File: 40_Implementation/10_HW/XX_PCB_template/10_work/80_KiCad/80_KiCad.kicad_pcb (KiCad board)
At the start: 4 copper layers, 68.6 x 53.3 mm, 37 parts, among them J1 Power, J2 Digital/PWM, J3 Analog, J4 Digital/PWM, J5 Conn_01x03_Socket, SW1 SW_SPST, U1 OPA340P, U2 OPA340P

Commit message: v1.1
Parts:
- added A2_Out1: TP_Vout2, Connector_PinHeader_2.54mm:PinHeader_1x01_P2.54mm_Vertical, F.Cu at (112.6, 97.1)
- added A_In1_N1: TP_A_in1_N, Connector_PinHeader_2.54mm:PinHeader_1x01_P2.54mm_Vertical, F.Cu at (102.5, 65.8)
- added A_In2_N1: TP_A_in2_N, Connector_PinHeader_2.54mm:PinHeader_1x01_P2.54mm_Vertical, F.Cu at (104.8, 96.9)
- added A_In_P1: TP_A_in_P, Connector_PinHeader_2.54mm:PinHeader_1x01_P2.54mm_Vertical, F.Cu at (102.8, 88.3)
- A1_Out1: value Vout Intermediate -> TP_Vout1
- GND2, GND3: value GND -> TP_GND
- V_In1: value Vin -> TP_Vin
- V_Out1: value Vout -> TP_Vout
- moved V_Out1 19.3 mm to (121.9, 97.5)
- moved GND3 9.60 mm to (102.6, 74.9)
- moved GND1 7.91 mm to (102.9, 59.1)
- moved A1_Out1 6.48 mm to (102.8, 82.5)
- moved VCC1 6.11 mm to (102.8, 52.4)
- moved D1 1.77 mm to (108.0, 54.4), turned to 0 degrees
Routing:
- net Net-(U1--): track 20.3 -> 58.6 mm
- net Net-(A2_Out1-Pad1): track 22.0 -> 52.2 mm
- net Net-(U2--): track 50.9 -> 75.9 mm
- net Vout: track 54.4 -> 36.6 mm
- net Net-(U1-+): track 92.1 -> 105.6 mm
- net Net-(A1_Out1-Pad1): track 59.4 -> 56.5 mm
- net Net-(D1-K): track 7.95 -> 9.81 mm
- net Red: track 40.9 -> 39.9 mm
- net GND: vias 1 -> 5

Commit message: v1.1.1
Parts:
- renumbered GND3 to GND, GND2 to GND, GND1 to GND
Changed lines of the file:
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@@
 		(descr "Through hole straight pin header, 1x01, 2.54mm pitch, single row")
 		(tags "Through hole pin header THT 1x01 2.54mm single row")
-		(property "Reference" "GND3"
+		(property "Reference" "GND"
 			(at 0 -3 0)
 			(layer "F.SilkS")
@@
 		(descr "Through hole straight pin header, 1x01, 2.54mm pitch, single row")
 		(tags "Through hole pin header THT 1x01 2.54mm single row")
-		(property "Reference" "GND2"
+		(property "Reference" "GND"
 			(at 0 -2.33 0)
 			(layer "F.SilkS")
@@
 		(descr "Through hole straight pin header, 1x01, 2.54mm pitch, single row")
 		(tags "Through hole pin header THT 1x01 2.54mm single row")
-		(property "Reference" "GND1"
+		(property "Reference" "GND"
 			(at 0 -3 0)
 			(layer "F.SilkS")

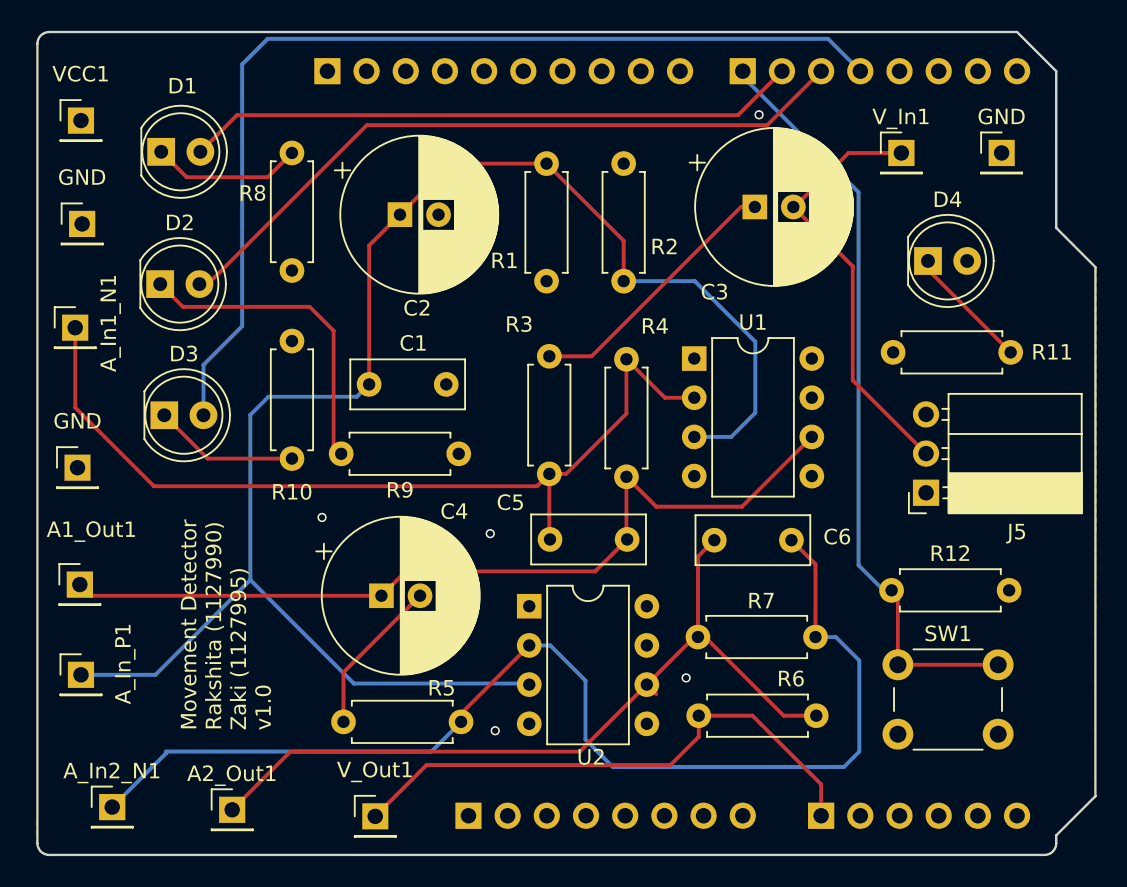
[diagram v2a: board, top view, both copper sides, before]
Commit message: Changed References - Silk Layer
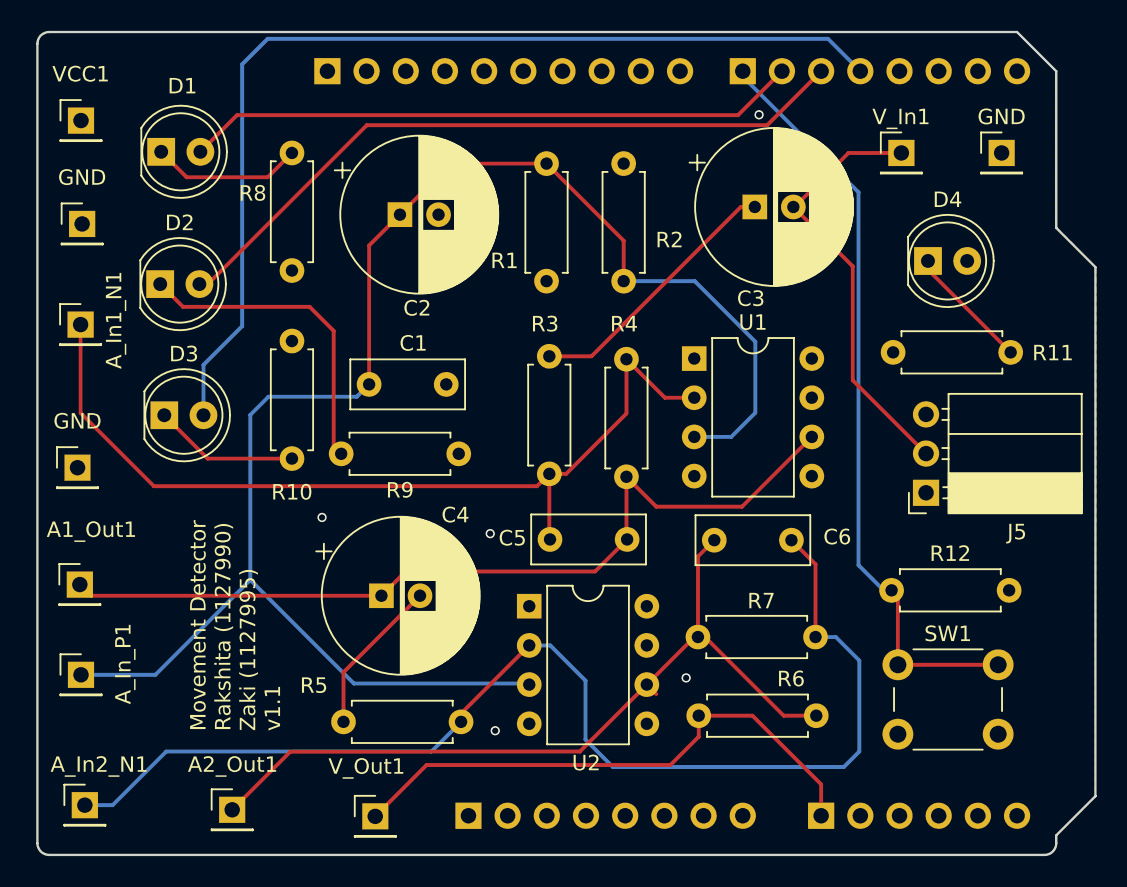
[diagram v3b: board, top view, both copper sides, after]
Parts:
- moved A_In2_N1 1.78 mm to (103.1, 96.8)
- moved A_In1_N1 0.40 mm to (102.8, 65.6)
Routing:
- net Net-(U2--): track 75.9 -> 77.5 mm
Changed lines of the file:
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@@
 		(title "Movement Detector")
 		(date "2024-05-05")
-		(rev "v1.0")
+		(rev "v1.1")
 		(company "Hochschule Darmstadt")
 	)
@@
 	(footprint "Connector_PinHeader_2.54mm:PinHeader_1x01_P2.54mm_Vertical"
 		(layer "F.Cu")
-		(at 102.45 65.825)
+		(at 102.8 65.625)
 		(descr "Through hole straight pin header, 1x01, 2.54mm pitch, single row")
 		(tags "Through hole pin header THT 1x01 2.54mm single row")
@@
 		(tags "C Rect series Radial pin pitch 5.00mm  length 7.2mm width 3.0mm Capacitor")
 		(property "Reference" "C5"
-			(at -2.55 -2.375 0)
+			(at -2.425 -0.075 0)
 			(layer "F.SilkS")
 			(effects
@@
 		(tags "Resistor Axial_DIN0207 series Axial Horizontal pin pitch 7.62mm 0.25W = 1/4W length 6.3mm diameter 2.5mm")
 		(property "Reference" "R3"
-			(at -2.055 1.955 180)
+			(at -2.08 0.28 180)
 			(layer "F.SilkS")
 			(effects
@@
 		(tags "THT DIP DIL PDIP 2.54mm 7.62mm 300mil")
 		(property "Reference" "U2"
-			(at 4.02 9.795 0)
+			(at 3.695 10.17 0)
 			(layer "F.SilkS")
 			(effects
@@
 		(tags "Through hole pin header THT 1x01 2.54mm single row")
 		(property "Reference" "V_Out1"
-			(at 0 -3 0)
+			(at -0.55 -3.225 0)
 			(layer "F.SilkS")
 			(effects
@@
 		(tags "Resistor Axial_DIN0207 series Axial Horizontal pin pitch 7.62mm 0.25W = 1/4W length 6.3mm diameter 2.5mm")
 		(property "Reference" "R5"
-			(at 6.36 -2.175 0)
+			(at -1.915 -2.35 0)
 			(layer "F.SilkS")
 			(effects
@@
 		(tags "Through hole pin header THT 1x01 2.54mm single row")
 		(property "Reference" "A2_Out1"
-			(at 0 -2.33 0)
+			(at 0.05 -2.925 0)
 			(layer "F.SilkS")
 			(effects
@@
 		(tags "Resistor Axial_DIN0207 series Axial Horizontal pin pitch 7.62mm 0.25W = 1/4W length 6.3mm diameter 2.5mm")
 		(property "Reference" "R11"
-			(at -2.69 0 180)
+			(at -2.74 -0.05 180)
 			(layer "F.SilkS")
 			(effects
@@
 		(tags "Resistor Axial_DIN0207 series Axial Horizontal pin pitch 7.62mm 0.25W = 1/4W length 6.3mm diameter 2.5mm")
 		(property "Reference" "R4"
-			(at -2.12 -1.845 180)
+			(at -2.27 0.155 180)
 			(layer "F.SilkS")
 			(effects
@@
 		(tags "Resistor Axial_DIN0207 series Axial Horizontal pin pitch 7.62mm 0.25W = 1/4W length 6.3mm diameter 2.5mm")
 		(property "Reference" "R2"
-			(at 2.21 2.65 0)
+			(at 2.66 2.975 0)
 			(layer "F.SilkS")
 			(effects
@@
 		(tags "CP Radial series Radial pin pitch 2.50mm  diameter 10mm Electrolytic Capacitor")
 		(property "Reference" "C3"
-			(at -2.6 5.525 0)
+			(at -0.25 5.95 0)
 			(layer "F.SilkS")
 			(effects
@@
 	(footprint "Connector_PinHeader_2.54mm:PinHeader_1x01_P2.54mm_Vertical"
 		(layer "F.Cu")
-		(at 104.85 96.9)
+		(at 103.075 96.775)
 		(descr "Through hole straight pin header, 1x01, 2.54mm pitch, single row")
 		(tags "Through hole pin header THT 1x01 2.54mm single row")
 		(property "Reference" "A_In2_N1"
-			(at 0 -2.33 0)
+			(at 0.95 -2.625 0)
 			(layer "F.SilkS")
 			(effects
@@
 		(tags "CP Radial series Radial pin pitch 2.50mm  diameter 10mm Electrolytic Capacitor")
 		(property "Reference" "C4"
-			(at 4.725 -5.45 0)
+			(at 4.8 -5.225 0)
 			(layer "F.SilkS")
 			(effects
@@
 	)
 	(gr_text "Movement Detector\nRakshita (1127990)\nZaki (1127995)\n${REVISION}"
-		(at 115.25 91.925 90)
+		(at 115.85 91.975 90)
 		(layer "F.SilkS")
 		(effects
@@
 	)
 	(segment
+		(start 102.8 71.35)
+		(end 102.8 65.625)
+		(width 0.25)
+		(layer "F.Cu")
+		(net 35)
+	)
+	(segment
 		(start 138.18 71.395)
 		(end 134.275 75.3)
@@
 	(segment
 		(start 107.549999 76.099999)
-		(end 102.45 71)
+		(end 102.8 71.35)
 		(width 0.25)
 		(layer "F.Cu")
@@
 	)
 	(segment
-		(start 102.45 71)
-		(end 102.45 65.825)
-		(width 0.25)
-		(layer "F.Cu")
-		(net 35)
-	)
-	(segment
 		(start 143.275 85.875)
 		(end 142.815 85.875)
@@
 	)
 	(segment
+		(start 108.35 93.3)
+		(end 104.875 96.775)
+		(width 0.25)
+		(layer "B.Cu")
+		(net 37)
+	)
+	(segment
 		(start 152.275 94.3)
 		(end 153.275 93.3)
@@
 	)
 	(segment
-		(start 108.35 93.4)
-		(end 104.85 96.9)
-		(width 0.25)
-		(layer "B.Cu")
-		(net 37)
-	)
-	(segment
 		(start 153.275 87.4)
 		(end 151.75 85.875)
@@
 	)
 	(segment
-		(start 108.35 93.3)
-		(end 108.35 93.4)
+		(start 104.875 96.775)
+		(end 103.075 96.775)
 		(width 0.25)
 		(layer "B.Cu")

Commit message: Changed References - Silk Layer - Minor Changes
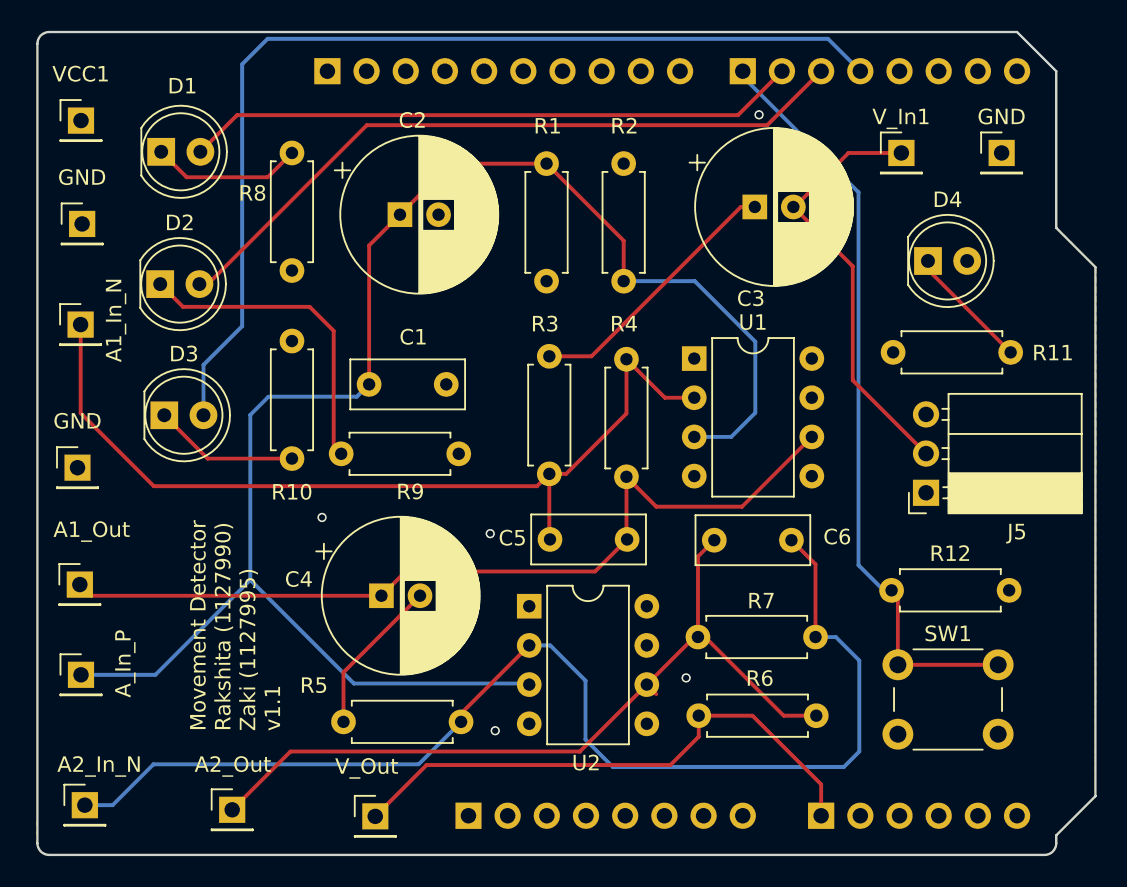
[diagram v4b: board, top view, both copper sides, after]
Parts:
- renumbered A_In1_N1 to A1_In_N, A1_Out1 to A1_Out, A_In2_N1 to A2_In_N, A2_Out1 to A2_Out, A_In_P1 to A_In_P, V_Out1 to V_Out
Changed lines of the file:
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@@
 		(tags "CP Radial series Radial pin pitch 2.50mm  diameter 10mm Electrolytic Capacitor")
 		(property "Reference" "C2"
-			(at 1.125 6.075 0)
+			(at 0.825 -6.1 0)
 			(layer "F.SilkS")
 			(effects
@@
 		(tags "Resistor Axial_DIN0207 series Axial Horizontal pin pitch 7.62mm 0.25W = 1/4W length 6.3mm diameter 2.5mm")
 		(property "Reference" "R9"
-			(at 3.81 -2.37 180)
+			(at 3.135 -2.475 180)
 			(layer "F.SilkS")
 			(effects
@@
 		(descr "Through hole straight pin header, 1x01, 2.54mm pitch, single row")
 		(tags "Through hole pin header THT 1x01 2.54mm single row")
-		(property "Reference" "A_In_P1"
-			(at 2.75 -0.725 -90)
+		(property "Reference" "A_In_P"
+			(at 2.75 -0.725 270)
 			(layer "F.SilkS")
 			(effects
@@
 		(descr "Through hole straight pin header, 1x01, 2.54mm pitch, single row")
 		(tags "Through hole pin header THT 1x01 2.54mm single row")
-		(property "Reference" "A_In1_N1"
-			(at 2.175 -0.3 -90)
+		(property "Reference" "A1_In_N"
+			(at 2.175 -0.3 270)
 			(layer "F.SilkS")
 			(effects
@@
 		(tags "Resistor Axial_DIN0207 series Axial Horizontal pin pitch 7.62mm 0.25W = 1/4W length 6.3mm diameter 2.5mm")
 		(property "Reference" "R1"
-			(at 1.31 -2.725 0)
+			(at 10.035 0.075 0)
 			(layer "F.SilkS")
 			(effects
@@
 		(descr "Through hole straight pin header, 1x01, 2.54mm pitch, single row")
 		(tags "Through hole pin header THT 1x01 2.54mm single row")
-		(property "Reference" "V_Out1"
+		(property "Reference" "V_Out"
 			(at -0.55 -3.225 0)
 			(layer "F.SilkS")
@@
 		(descr "Through hole straight pin header, 1x01, 2.54mm pitch, single row")
 		(tags "Through hole pin header THT 1x01 2.54mm single row")
-		(property "Reference" "A2_Out1"
+		(property "Reference" "A2_Out"
 			(at 0.05 -2.925 0)
 			(layer "F.SilkS")
@@
 		(tags "C Rect series Radial pin pitch 5.00mm  length 7.2mm width 3.0mm Capacitor")
 		(property "Reference" "C1"
-			(at 2.875 -2.65 0)
+			(at 2.875 -3.05 0)
 			(layer "F.SilkS")
 			(effects
@@
 		(descr "Through hole straight pin header, 1x01, 2.54mm pitch, single row")
 		(tags "Through hole pin header THT 1x01 2.54mm single row")
-		(property "Reference" "A1_Out1"
+		(property "Reference" "A1_Out"
 			(at 0.775 -3.55 0)
 			(layer "F.SilkS")
@@
 		(tags "Resistor Axial_DIN0207 series Axial Horizontal pin pitch 7.62mm 0.25W = 1/4W length 6.3mm diameter 2.5mm")
 		(property "Reference" "R6"
-			(at 1.635 2.375 180)
+			(at 3.66 2.4 180)
 			(layer "F.SilkS")
 			(effects
@@
 		(tags "Resistor Axial_DIN0207 series Axial Horizontal pin pitch 7.62mm 0.25W = 1/4W length 6.3mm diameter 2.5mm")
 		(property "Reference" "R2"
-			(at 2.66 2.975 0)
+			(at 10.035 0.05 0)
 			(layer "F.SilkS")
 			(effects
@@
 		(descr "Through hole straight pin header, 1x01, 2.54mm pitch, single row")
 		(tags "Through hole pin header THT 1x01 2.54mm single row")
-		(property "Reference" "A_In2_N1"
+		(property "Reference" "A2_In_N"
 			(at 0.95 -2.625 0)
 			(layer "F.SilkS")
@@
 		(tags "CP Radial series Radial pin pitch 2.50mm  diameter 10mm Electrolytic Capacitor")
 		(property "Reference" "C4"
-			(at 4.8 -5.225 0)
+			(at -5.35 -1.05 0)
 			(layer "F.SilkS")
 			(effects
@@
 	)
 	(segment
-		(start 108.35 93.3)
-		(end 104.875 96.775)
+		(start 124.71 94.125)
+		(end 107.525 94.125)
 		(width 0.25)
 		(layer "B.Cu")
@@
 	)
 	(segment
-		(start 125.535 93.3)
-		(end 108.35 93.3)
+		(start 135.525 92.525)
+		(end 137.3 94.3)
 		(width 0.25)
 		(layer "B.Cu")
@@
 	)
 	(segment
-		(start 135.525 92.525)
-		(end 137.3 94.3)
+		(start 127.46 91.375)
+		(end 124.71 94.125)
 		(width 0.25)
 		(layer "B.Cu")
@@
 	)
 	(segment
-		(start 127.46 91.375)
-		(end 125.535 93.3)
+		(start 104.875 96.775)
+		(end 103.075 96.775)
 		(width 0.25)
 		(layer "B.Cu")
@@
 	)
 	(segment
-		(start 104.875 96.775)
-		(end 103.075 96.775)
+		(start 107.525 94.125)
+		(end 104.875 96.775)
 		(width 0.25)
 		(layer "B.Cu")

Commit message: After capacitor change - 21.05s
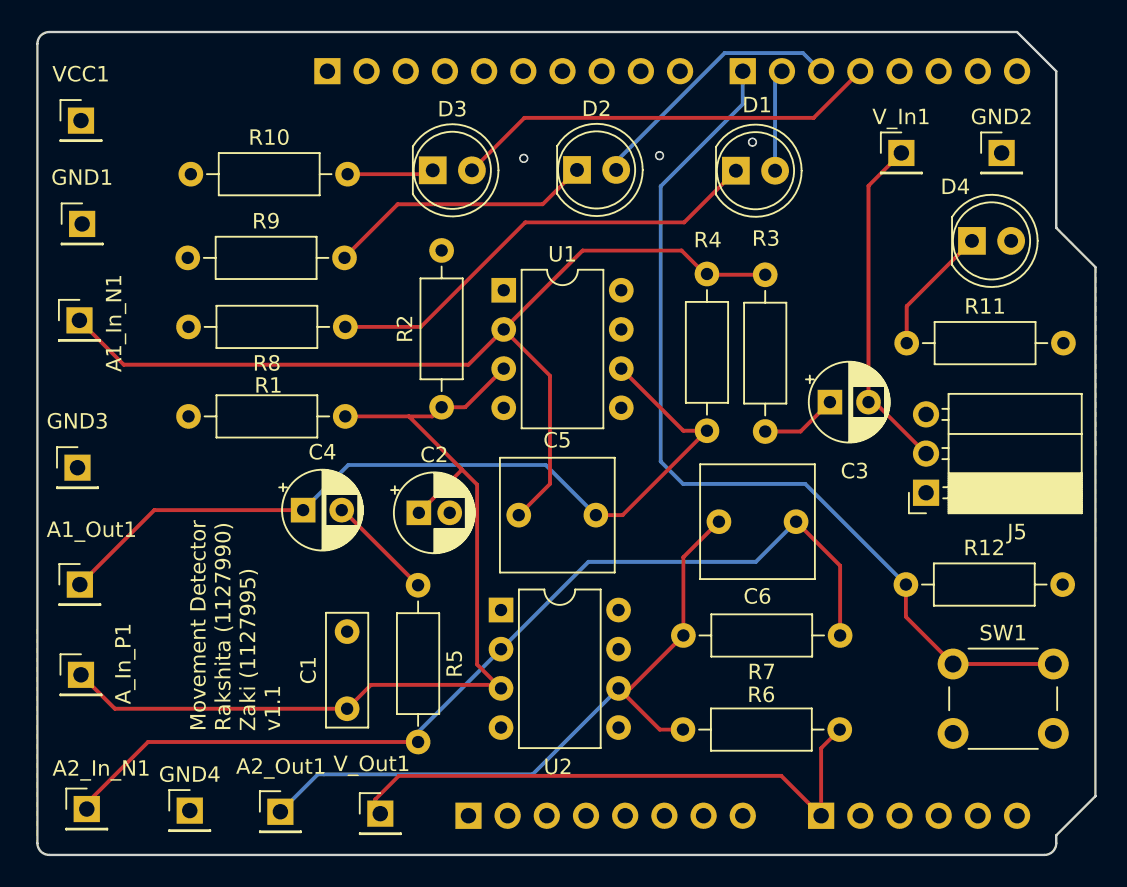
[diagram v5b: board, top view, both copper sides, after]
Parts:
- added GND4: TP_GND, Connector_PinHeader_2.54mm:PinHeader_1x01_P2.54mm_Vertical, F.Cu at (109.9, 97.1)
- A1_In_N1: renamed from A1_In_N; value TP_A_in1_N -> TP_A1_In_N
- A2_In_N1: renamed from A2_In_N; value TP_A_in2_N -> TP_A2_In_N
- C1: footprint Capacitor_THT:C_Rect_L7.2mm_W3.0mm_P5.00mm_FKS2_FKP2_MKS2_MKP2 -> Capacitor_THT:C_Rect_L7.2mm_W2.5mm_P5.00mm_FKS2_FKP2_MKS2_MKP2
- C2: footprint Capacitor_THT:CP_Radial_D10.0mm_P2.50mm -> Capacitor_THT:CP_Radial_D5.0mm_P2.00mm
- C3, C4: footprint Capacitor_THT:CP_Radial_D10.0mm_P2.50mm -> Capacitor_THT:CP_Radial_D5.0mm_P2.50mm
- C5, C6: footprint Capacitor_THT:C_Rect_L7.2mm_W3.0mm_P5.00mm_FKS2_FKP2_MKS2_MKP2 -> Capacitor_THT:C_Rect_L7.2mm_W7.2mm_P5.00mm_FKS2_FKP2_MKS2_MKP2
- R1, R10, R11, R12, R2, R3, R4, R5, R6, R7, R8, R9: footprint Resistor_THT:R_Axial_DIN0207_L6.3mm_D2.5mm_P7.62mm_Horizontal -> Resistor_THT:R_Axial_DIN0207_L6.3mm_D2.5mm_P10.16mm_Horizontal
- SW1: footprint Button_Switch_THT:SW_PUSH_6mm -> Button_Switch_THT:SW_PUSH_6mm_H7.3mm
- moved D1 37.3 mm to (145.3, 55.6)
- moved D2 28.0 mm to (135.0, 55.6)
- moved R1 24.8 mm to (109.8, 71.6), turned to 0 degrees
- moved D3 23.6 mm to (125.6, 55.6)
- moved R9 21.7 mm to (109.7, 61.3), turned to 0 degrees
- moved C1 21.1 mm to (120.1, 90.5), turned to 90 degrees
- moved C2 19.4 mm to (124.7, 77.8)
- moved R3 14.8 mm to (147.2, 72.6), turned to 90 degrees
- moved R2 14.4 mm to (126.2, 71.0)
- moved C3 13.6 mm to (151.4, 70.7)
- moved U1 13.1 mm to (130.2, 63.4)
- moved R10 12.6 mm to (109.9, 55.9), turned to 0 degrees
- moved R8 11.8 mm to (120.0, 65.8), turned to 180 degrees
- moved R5 10.1 mm to (124.7, 82.5), turned to -90 degrees
- moved R6 8.69 mm to (141.8, 91.9), turned to 0 degrees
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- renumbered A1_Out to A1_Out1, A2_Out to A2_Out1, A_In_P to A_In_P1, GND to GND1, GND to GND2, GND to GND3, V_Out to V_Out1
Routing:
- net Net-(U1-+): track 105.6 -> 64.5 mm
- net Green: track 65.4 -> 27.8 mm
- net Red: track 39.9 -> 6.63 mm
- net Orange: track 46.0 -> 17.2 mm
- net Net-(D1-K): track 9.81 -> 29.5 mm
- net Net-(U2--): track 77.5 -> 62.6 mm
- net Net-(C3-Pad1): track 17.3 -> 4.98 mm
- net Push Button: track 50.1 -> 60.0 mm
- net Net-(A2_Out1-Pad1): track 52.2 -> 44.7 mm
- net Vin: track 28.0 -> 22.1 mm
- net Net-(U1--): track 58.7 -> 63.5 mm
- net Net-(D3-K): track 9.44 -> 5.62 mm
- net Net-(C4-Pad2): track 10.2 -> 6.97 mm
- net Net-(D2-K): track 20.7 -> 17.4 mm
- net Vout: track 36.6 -> 38.2 mm
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
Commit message: 22.05
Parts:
- moved GND2 38.4 mm to (164.5, 92.8)
- moved V_In1 38.3 mm to (156.7, 92.8)
- moved SW1 28.9 mm to (162.2, 58.9), turned to 180 degrees
- moved D4 25.9 mm to (160.8, 86.0)
- moved D1 19.8 mm to (125.5, 55.6)
- moved D3 19.5 mm to (145.1, 55.5)
- moved R12 18.7 mm to (154.5, 63.9)
- moved R11 13.4 mm to (156.5, 80.2)
- moved R10 10.5 mm to (109.7, 66.3)
- moved R8 10.1 mm to (120.1, 55.7)
- moved J5 2.68 mm to (157.6, 73.8)
- moved C4 1.16 mm to (116.1, 77.7)
- moved C2 0.56 mm to (124.2, 77.7)
- renumbered A1_In_N1 to A1_In_N, A1_Out1 to A1_Out, A2_In_N1 to A2_In_N, A2_Out1 to A2_Out, A_In_P1 to A_In_P, GND4 to GND, GND3 to GND, GND1 to GND, VCC1 to VCC, V_Out1 to V_Out
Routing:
- net Push Button: track 60.0 -> 26.9 mm
- net Net-(D3-K): track 5.62 -> 30.8 mm
- net Net-(D1-K): track 29.5 -> 5.77 mm
- net Green: track 27.8 -> 8.65 mm
- net Red: track 6.63 -> 23.5 mm
- net Vin: track 22.1 -> 27.7 mm
- net Net-(U1-+): track 64.5 -> 68.3 mm
- net Net-(C4-Pad2): track 6.97 -> 8.10 mm
- net Orange: track 17.2 -> 16.5 mm
- net GND: vias 3 -> 0
